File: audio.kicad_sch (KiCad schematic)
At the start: 11 parts, among them Q8 BSS138, U7 LM4990MM, U8 MAX9814

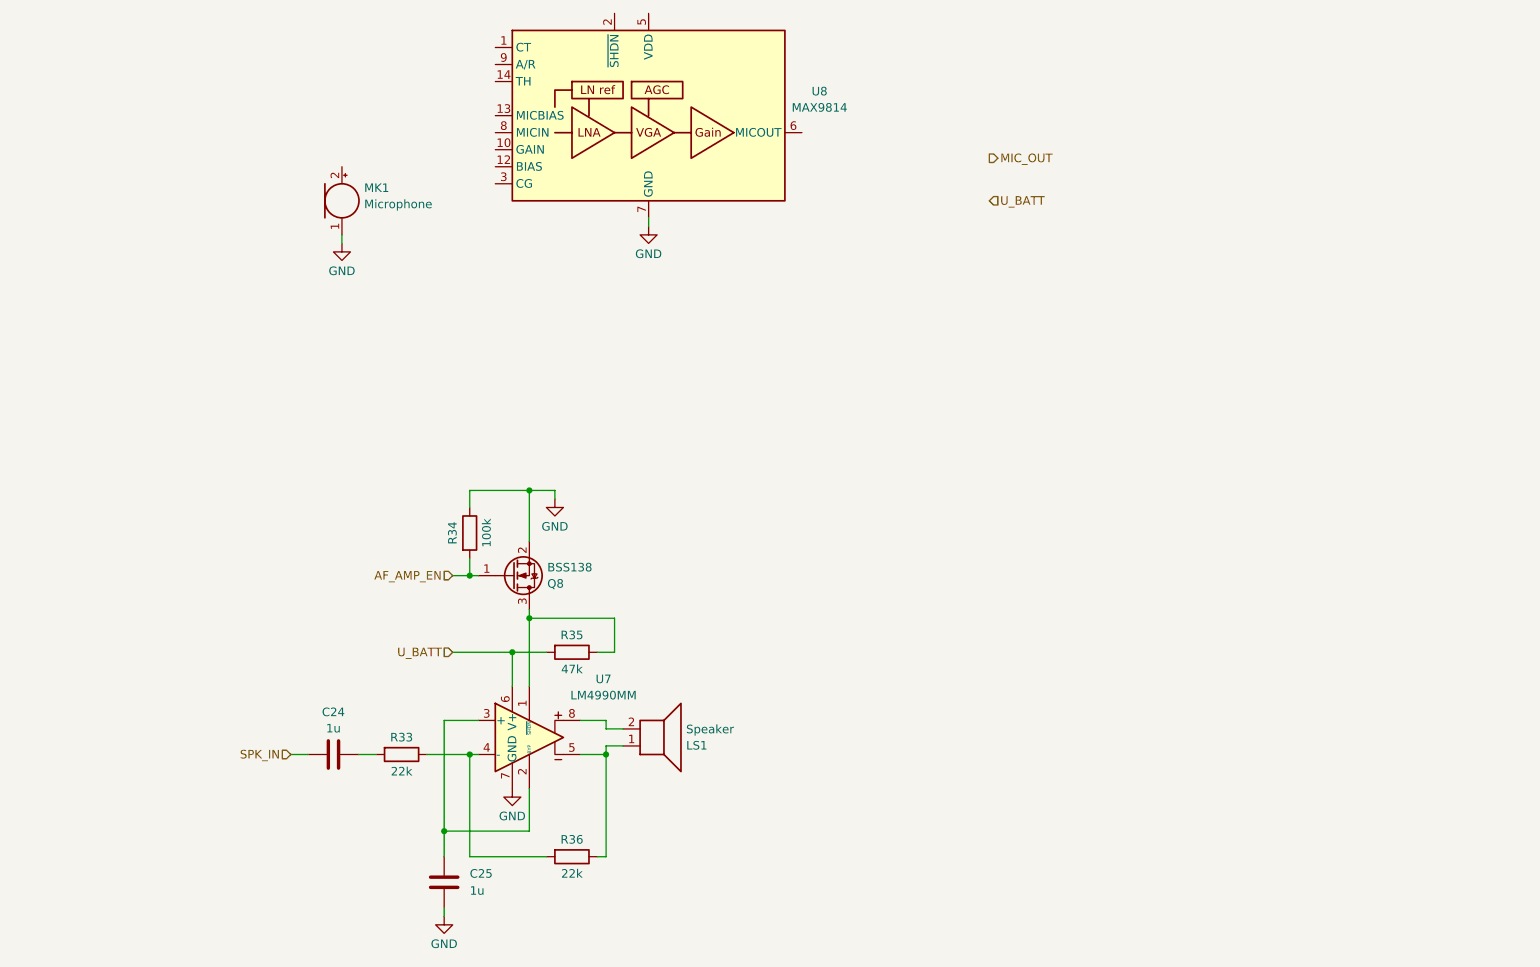
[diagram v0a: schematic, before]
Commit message: spk/mic update
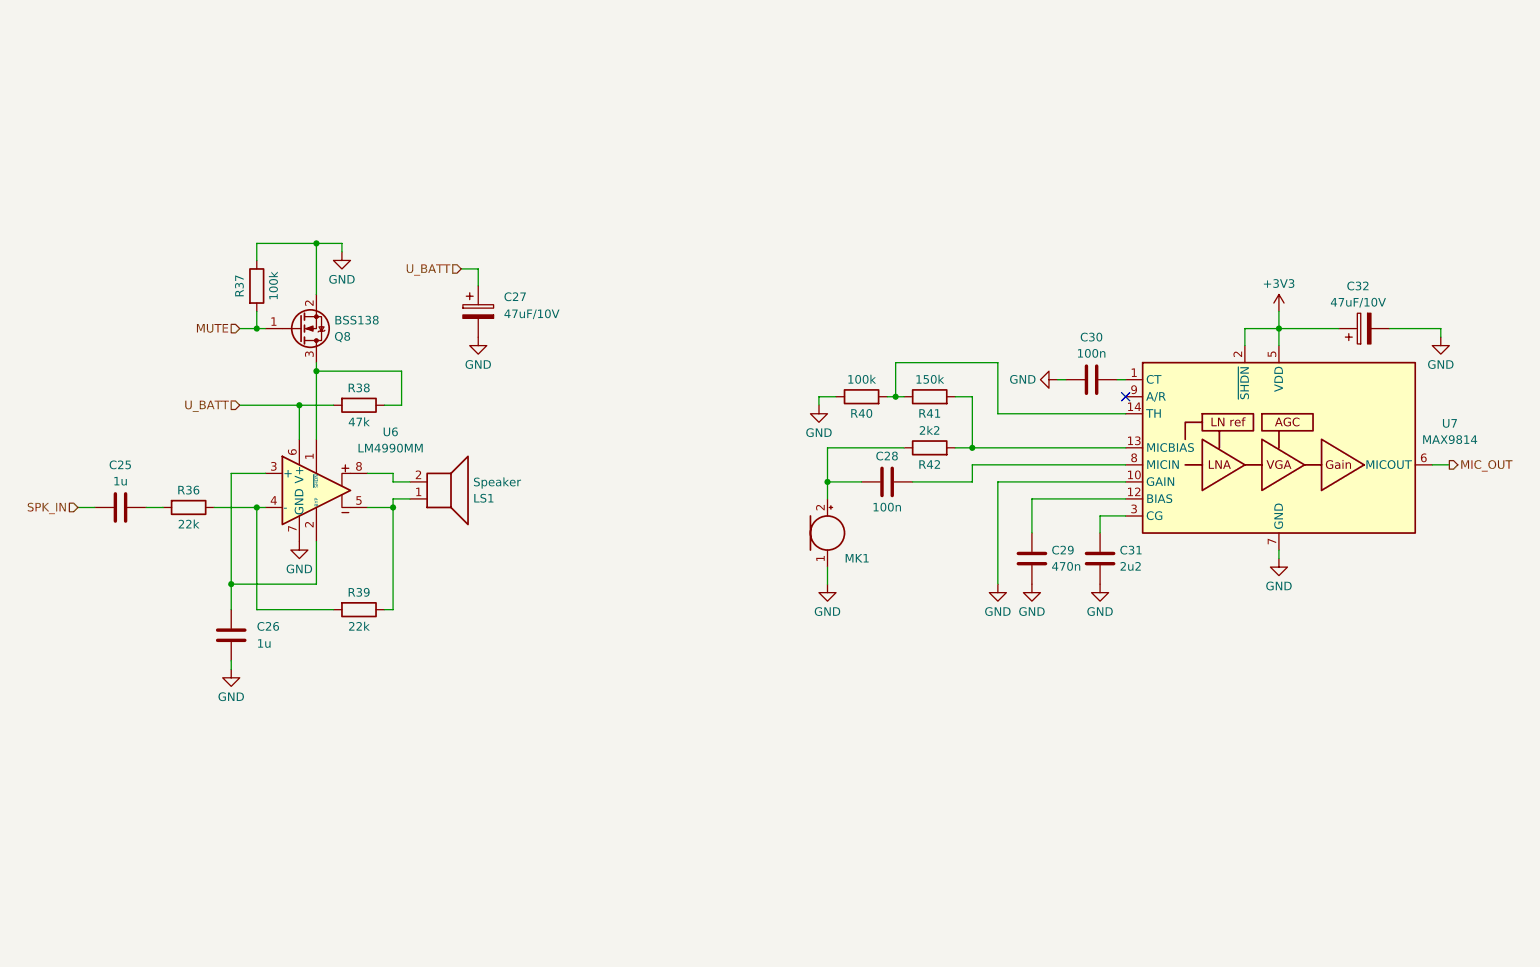
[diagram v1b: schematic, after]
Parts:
- added C27, C32: 47uF/10V, Capacitor_Tantalum_SMD:CP_EIA-3528-21_Kemet-B, symbol Device:C_Polarized
- added C28, C30: 100n, Capacitor_SMD:C_0805_2012Metric, symbol Device:C
- added C29: 470n, Capacitor_SMD:C_0805_2012Metric, symbol Device:C
- added C31: 2u2, Capacitor_SMD:C_0805_2012Metric, symbol Device:C
- added R40: 100k, Inductor_SMD:L_0805_2012Metric, symbol Device:R
- added R41: 150k, Inductor_SMD:L_0805_2012Metric, symbol Device:R
- added R42: 2k2, Inductor_SMD:L_0805_2012Metric, symbol Device:R
- renumbered C24 to C25, C25 to C26, R33 to R36, R34 to R37, R35 to R38, R36 to R39, U7 to U6, U8 to U7
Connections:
- net GND: now also U7.10 (GAIN), C27.2, C29.2, C30.1, C31.2, C32.2, R40.1
- net MIC_OUT: now also U7.6 (MICOUT)
- net U_BATT: now also C27.1
- net at MK1.2 (+): now also C28.1, R42.1
- net at U7.1 (CT): now also C30.2
- net at U7.12 (BIAS): now also C29.1
- net at U7.13 (MICBIAS): now also R41.2, R42.2
- net at U7.14 (TH): now also R40.2, R41.1
- net +3V3: now reaches U7.2 (~{SHDN})
- net +3V3: now also U7.5 (VDD), C32.1
- net at U7.3 (CG): now also C31.1
- net at U7.8 (MICIN): now also C28.2
- net AF_AMP_EN renamed MUTE
- no-connect marks 0 -> 1
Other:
- moved on the sheet: C25, C26, LS1, MK1, Q8, R36, R37, R38, R39, U6, U7

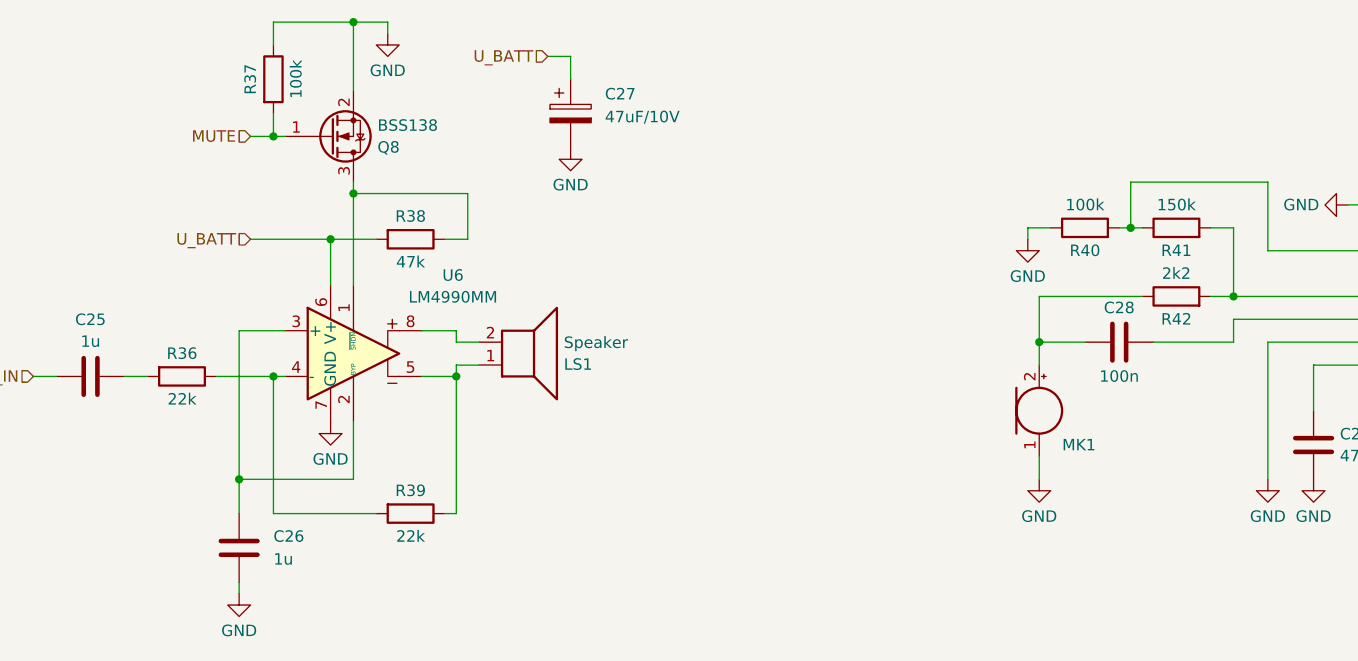
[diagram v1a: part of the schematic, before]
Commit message: removed audio part
- added buzzer
- added battery voltage measurement
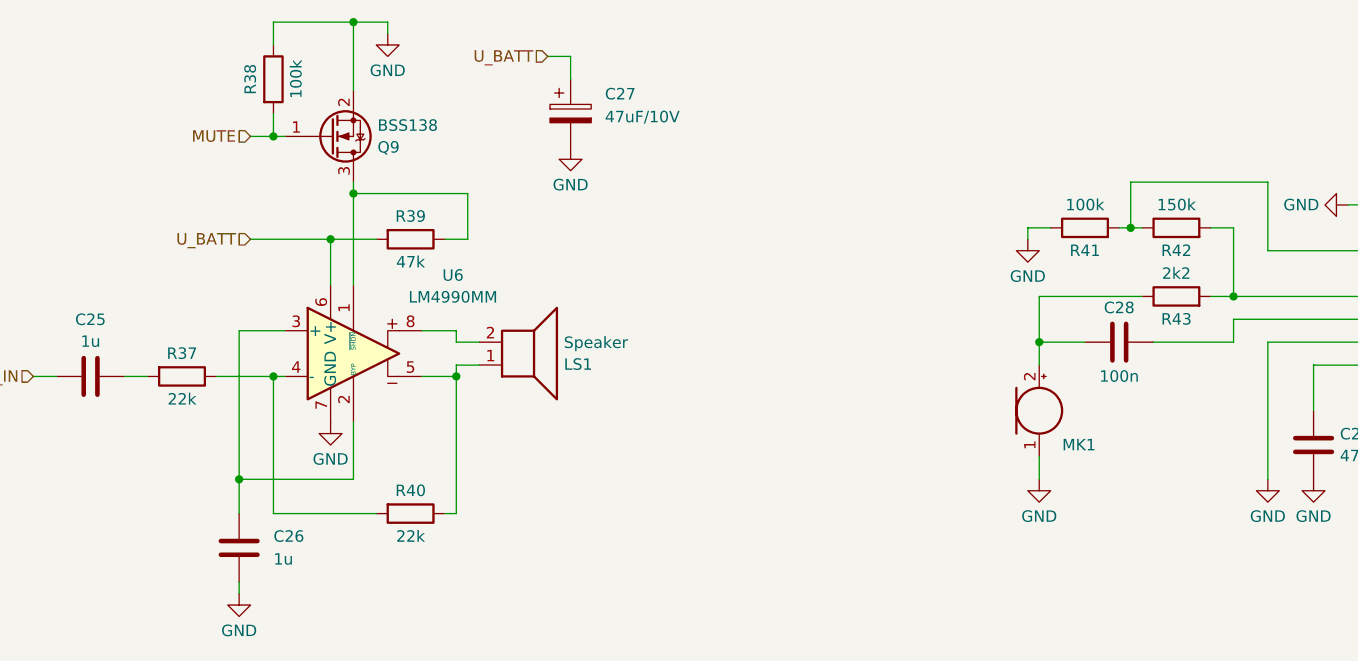
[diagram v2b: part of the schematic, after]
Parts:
- renumbered Q8 to Q9, R36 to R37, R37 to R38, R38 to R39, R39 to R40, R40 to R41, R41 to R42, R42 to R43
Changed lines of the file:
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@@
 	(title_block
 		(title "Mainboard replacement for Nokia 3310")
-		(date "28-10-2024")
+		(date "29-10-2024")
 		(rev "Rev A")
 		(company "M17 Project")
@@
 		(dnp no)
 		(fields_autoplaced yes)
-		(property "Reference" "#PWR082"
+		(property "Reference" "#PWR083"
 			(at 247.65 83.82 0)
 			(effects
@@
 			(project "M17_3310"
 				(path "/8d65c5ef-7a02-4454-aee5-ab9c49e4aeab/8834b759-9ccc-443c-b4d0-4a3047addc78"
-					(reference "#PWR082")
+					(reference "#PWR083")
 					(unit 1)
 				)
@@
 		(on_board yes)
 		(dnp no)
-		(property "Reference" "R41"
+		(property "Reference" "R42"
 			(at 171.45 88.9 90)
 			(effects
@@
 			(project "M17_3310"
 				(path "/8d65c5ef-7a02-4454-aee5-ab9c49e4aeab/8834b759-9ccc-443c-b4d0-4a3047addc78"
-					(reference "R41")
+					(reference "R42")
 					(unit 1)
 				)
@@
 		(dnp no)
 		(fields_autoplaced yes)
-		(property "Reference" "#PWR072"
+		(property "Reference" "#PWR073"
 			(at 83.82 71.12 0)
 			(effects
@@
 			(project "M17_3310"
 				(path "/8d65c5ef-7a02-4454-aee5-ab9c49e4aeab/8834b759-9ccc-443c-b4d0-4a3047addc78"
-					(reference "#PWR072")
+					(reference "#PWR073")
 					(unit 1)
 				)
@@
 		(dnp no)
 		(fields_autoplaced yes)
-		(property "Reference" "#PWR077"
+		(property "Reference" "#PWR078"
 			(at 186.69 120.65 0)
 			(effects
@@
 			(project "M17_3310"
 				(path "/8d65c5ef-7a02-4454-aee5-ab9c49e4aeab/8834b759-9ccc-443c-b4d0-4a3047addc78"
-					(reference "#PWR077")
+					(reference "#PWR078")
 					(unit 1)
 				)
@@
 		(dnp no)
 		(fields_autoplaced yes)
-		(property "Reference" "#PWR081"
+		(property "Reference" "#PWR082"
 			(at 223.52 116.84 0)
 			(effects
@@
 			(project "M17_3310"
 				(path "/8d65c5ef-7a02-4454-aee5-ab9c49e4aeab/8834b759-9ccc-443c-b4d0-4a3047addc78"
-					(reference "#PWR081")
+					(reference "#PWR082")
 					(unit 1)
 				)
@@
 		(on_board yes)
 		(dnp no)
-		(property "Reference" "R38"
+		(property "Reference" "R39"
 			(at 86.36 85.09 90)
 			(effects
@@
 			(project "M17_3310"
 				(path "/8d65c5ef-7a02-4454-aee5-ab9c49e4aeab/8834b759-9ccc-443c-b4d0-4a3047addc78"
-					(reference "R38")
+					(reference "R39")
 					(unit 1)
 				)
@@
 		(on_board yes)
 		(dnp no)
-		(property "Reference" "R36"
+		(property "Reference" "R37"
 			(at 60.96 100.33 90)
 			(effects
@@
 			(project "M17_3310"
 				(path "/8d65c5ef-7a02-4454-aee5-ab9c49e4aeab/8834b759-9ccc-443c-b4d0-4a3047addc78"
-					(reference "R36")
+					(reference "R37")
 					(unit 1)
 				)
@@
 		(on_board yes)
 		(dnp no)
-		(property "Reference" "R42"
+		(property "Reference" "R43"
 			(at 171.45 96.52 90)
 			(effects
@@
 			(project "M17_3310"
 				(path "/8d65c5ef-7a02-4454-aee5-ab9c49e4aeab/8834b759-9ccc-443c-b4d0-4a3047addc78"
-					(reference "R42")
+					(reference "R43")
 					(unit 1)
 				)
@@
 		(dnp no)
 		(fields_autoplaced yes)
-		(property "Reference" "#PWR079"
+		(property "Reference" "#PWR080"
 			(at 196.85 120.65 0)
 			(effects
@@
 			(project "M17_3310"
 				(path "/8d65c5ef-7a02-4454-aee5-ab9c49e4aeab/8834b759-9ccc-443c-b4d0-4a3047addc78"
-					(reference "#PWR079")
+					(reference "#PWR080")
 					(unit 1)
 				)
@@
 		(dnp no)
 		(fields_autoplaced yes)
-		(property "Reference" "#PWR076"
+		(property "Reference" "#PWR077"
 			(at 181.61 120.65 0)
 			(effects
@@
 			(project "M17_3310"
 				(path "/8d65c5ef-7a02-4454-aee5-ab9c49e4aeab/8834b759-9ccc-443c-b4d0-4a3047addc78"
-					(reference "#PWR076")
+					(reference "#PWR077")
 					(unit 1)
 				)
@@
 		(dnp no)
 		(fields_autoplaced yes)
-		(property "Reference" "#PWR075"
+		(property "Reference" "#PWR076"
 			(at 156.21 120.65 0)
 			(effects
@@
 			(project "M17_3310"
 				(path "/8d65c5ef-7a02-4454-aee5-ab9c49e4aeab/8834b759-9ccc-443c-b4d0-4a3047addc78"
-					(reference "#PWR075")
+					(reference "#PWR076")
 					(unit 1)
 				)
@@
 		(dnp no)
 		(fields_autoplaced yes)
-		(property "Reference" "#PWR078"
+		(property "Reference" "#PWR079"
 			(at 184.15 83.82 0)
 			(effects
@@
 			(project "M17_3310"
 				(path "/8d65c5ef-7a02-4454-aee5-ab9c49e4aeab/8834b759-9ccc-443c-b4d0-4a3047addc78"
-					(reference "#PWR078")
+					(reference "#PWR079")
 					(unit 1)
 				)
@@
 		(dnp no)
 		(fields_autoplaced yes)
-		(property "Reference" "#PWR080"
+		(property "Reference" "#PWR081"
 			(at 223.52 77.47 0)
 			(effects
@@
 			(project ""
 				(path "/8d65c5ef-7a02-4454-aee5-ab9c49e4aeab/8834b759-9ccc-443c-b4d0-4a3047addc78"
-					(reference "#PWR080")
+					(reference "#PWR081")
 					(unit 1)
 				)
@@
 		(dnp no)
 		(fields_autoplaced yes)
-		(property "Reference" "#PWR071"
+		(property "Reference" "#PWR072"
 			(at 77.47 114.3 0)
 			(effects
@@
 			(project "M17_3310"
 				(path "/8d65c5ef-7a02-4454-aee5-ab9c49e4aeab/8834b759-9ccc-443c-b4d0-4a3047addc78"
-					(reference "#PWR071")
+					(reference "#PWR072")
 					(unit 1)
 				)
@@
 		(on_board yes)
 		(dnp no)
-		(property "Reference" "Q8"
+		(property "Reference" "Q9"
 			(at 82.677 77.4122 0)
 			(effects
@@
 			(project ""
 				(path "/8d65c5ef-7a02-4454-aee5-ab9c49e4aeab/8834b759-9ccc-443c-b4d0-4a3047addc78"
-					(reference "Q8")
+					(reference "Q9")
 					(unit 1)
 				)
@@
 		(on_board yes)
 		(dnp no)
-		(property "Reference" "R37"
+		(property "Reference" "R38"
 			(at 68.58 69.85 90)
 			(effects
@@
 			(project "M17_3310"
 				(path "/8d65c5ef-7a02-4454-aee5-ab9c49e4aeab/8834b759-9ccc-443c-b4d0-4a3047addc78"
-					(reference "R37")
+					(reference "R38")
 					(unit 1)
 				)
@@
 		(dnp no)
 		(fields_autoplaced yes)
-		(property "Reference" "#PWR073"
+		(property "Reference" "#PWR074"
 			(at 104.14 83.82 0)
 			(effects
@@
 			(project "M17_3310"
 				(path "/8d65c5ef-7a02-4454-aee5-ab9c49e4aeab/8834b759-9ccc-443c-b4d0-4a3047addc78"
-					(reference "#PWR073")
+					(reference "#PWR074")
 					(unit 1)
 				)
@@
 		(on_board yes)
 		(dnp no)
-		(property "Reference" "R40"
+		(property "Reference" "R41"
 			(at 161.29 88.9 90)
 			(effects
@@
 			(project "M17_3310"
 				(path "/8d65c5ef-7a02-4454-aee5-ab9c49e4aeab/8834b759-9ccc-443c-b4d0-4a3047addc78"
-					(reference "R40")
+					(reference "R41")
 					(unit 1)
 				)
@@
 		(on_board yes)
 		(dnp no)
-		(property "Reference" "R39"
+		(property "Reference" "R40"
 			(at 86.36 115.57 90)
 			(effects
@@
 			(project "M17_3310"
 				(path "/8d65c5ef-7a02-4454-aee5-ab9c49e4aeab/8834b759-9ccc-443c-b4d0-4a3047addc78"
-					(reference "R39")
+					(reference "R40")
 					(unit 1)
 				)
@@
 		(dnp no)
 		(fields_autoplaced yes)
-		(property "Reference" "#PWR070"
+		(property "Reference" "#PWR071"
 			(at 67.31 133.35 0)
 			(effects
@@
 			(project ""
 				(path "/8d65c5ef-7a02-4454-aee5-ab9c49e4aeab/8834b759-9ccc-443c-b4d0-4a3047addc78"
-					(reference "#PWR070")
+					(reference "#PWR071")
 					(unit 1)
 				)
@@
 		(dnp no)
 		(fields_autoplaced yes)
-		(property "Reference" "#PWR074"
+		(property "Reference" "#PWR075"
 			(at 154.94 93.98 0)
 			(effects
@@
 			(project "M17_3310"
 				(path "/8d65c5ef-7a02-4454-aee5-ab9c49e4aeab/8834b759-9ccc-443c-b4d0-4a3047addc78"
-					(reference "#PWR074")
+					(reference "#PWR075")
 					(unit 1)
 				)
